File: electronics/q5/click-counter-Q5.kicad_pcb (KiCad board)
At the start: 2 copper layers, 42 x 54 mm, 93 parts, among them J1 USB-C power and DFU, Q1 Discharge FET, Q2 Charge FET, Q3 Charge enable, Q4 Charge enable hot gate, Q5 COUNT key level shift, SW1 COUNT / POWER, SW2 RESET COUNT / BOOT, SW3 MCU RESET, U1 STM32L072CBT6, U2 Li-ion charger, U3 3.20481V adjustable LDO, U4 Cell protector, U5 Push-pull temperature window, U6 OLED power slew switch, U7 System soft-power latch switch, U8 SPI F-RAM 32KiB

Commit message: WIP: Q5 design-lock routing iteration snapshot (not verified)
Co-Authored-By: Claude Opus 5.5 <noreply@anthropic.com>
Claude-Session: https://claude.ai/code/session_01UrkzLMrBi6iLPSL5SbMCA7
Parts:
- added C40: 4.7n, CountFidgetQ5:Capacitor_SMD_C_0603_1608Metric, B.Cu at (29.0, 37.0)
- added R38: 100k, CountFidgetQ5:Resistor_SMD_R_0603_1608Metric, B.Cu at (27.6, 37.3)
- SW1, SW2: footprint CountFidgetQ5:HanElectricity_CPG151101D13_MX_Plate -> CountFidgetQ5:SW_Hotswap_Kailh_MX_CPG151101S11; moved to B.Cu
- moved C29 15.0 mm to (28.9, 44.2)
- moved TP12 14.4 mm to (23.4, 43.6)
- moved R35 13.0 mm to (31.1, 30.0), turned to 180 degrees
- moved Q3 8.40 mm to (2.29, 47.5), turned to 90 degrees
- moved U3 7.72 mm to (39.3, 48.1)
- moved R11 6.20 mm to (2.47, 44.8), turned to 180 degrees
- moved TP11 6.00 mm to (28.3, 47.8)
- moved SW1 5.68 mm to (11.5, 40.8), turned to 90 degrees
- moved SW2 5.68 mm to (30.5, 40.8), turned to -90 degrees
- moved R10 4.60 mm to (6.40, 50.9)
- moved TP6 4.40 mm to (27.3, 40.2)
- moved C39 4.40 mm to (26.1, 37.0)
- moved SW3 4.22 mm to (33.6, 51.2)
- moved U5 4.00 mm to (9.28, 51.3), turned to 180 degrees
- moved C6 4.00 mm to (38.9, 40.6)
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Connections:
- D4 pad 1: SYS_ON -> VBUS_WAKE
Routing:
- net GND: track 368.8 -> 0.00 mm, vias 36 -> 0
- net VLOGIC: track 158.4 -> 0.00 mm, vias 4 -> 0
- net VBUS: track 123.4 -> 0.00 mm, vias 7 -> 0
- net SYS: track 103.0 -> 0.00 mm, vias 5 -> 0
- net BOOT_COUNT_RESET: track 92.0 -> 0.00 mm, vias 2 -> 0
- net SYS_LOAD: track 72.9 -> 0.00 mm, vias 3 -> 0
- net SYS_ON: track 71.5 -> 0.00 mm, vias 4 -> 0
- net CE_N: track 70.1 -> 0.00 mm, vias 2 -> 0
- net OLED_RESET_N: track 51.2 -> 0.00 mm, vias 1 -> 0
- net OLED_ENABLE: track 48.1 -> 0.00 mm
- net OLED_CS_N: track 47.1 -> 0.00 mm, vias 1 -> 0
- net CHG_STAT1: track 45.2 -> 0.00 mm, vias 2 -> 0
- net NRST: track 44.1 -> 0.00 mm, vias 4 -> 0
- net CELL_P: track 42.8 -> 0.00 mm
- net TEMP_SENSE: track 32.9 -> 0.00 mm, vias 2 -> 0
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- removed copper zone on B.Cu, net GND
- removed copper zone on F.Cu, net GND

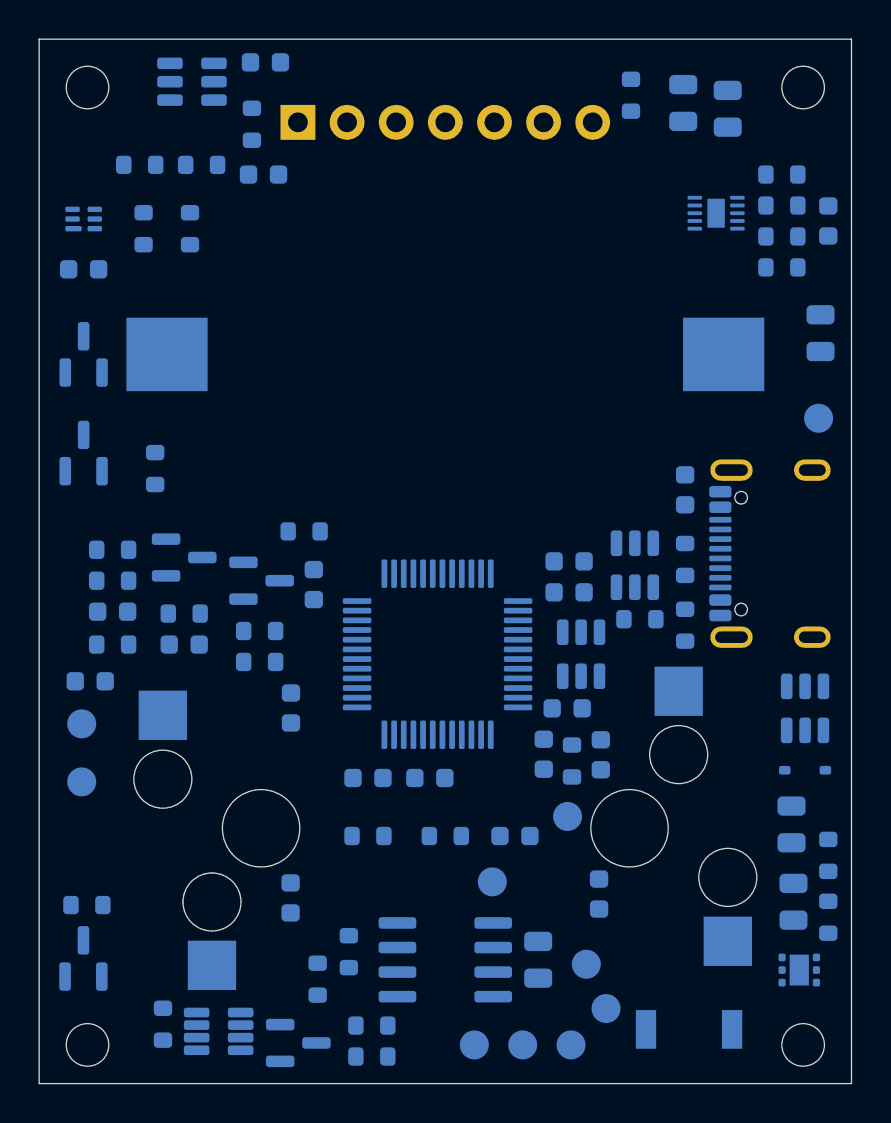
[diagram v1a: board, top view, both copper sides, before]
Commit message: Q5 design lock (electronics): hot-swap sockets, latch filter, 1.6 mm, clean native verification
Independent hardware/DFM and mechanical review follow-up:
- SW1/SW2 are now vendor-SMT Kailh-type MX hot-swap sockets (CPG151101S11-16,
  C41430893, rotated outward). The clicky switches clip into the printed
  plate and press in, so JLC can solder every part (variant B) and no switch
  soldering is needed in either variant. The board is 1.6 mm (MX pin length).
- R38 100k series + C40 4.7nF on U7 ON: VBUS hot-plug filter below the 6 V
  abs max and a contact-bounce bridge.
- BT1: +/- polarity silkscreen outside the holder body and paste kept off
  the inboard land; J1 slot rings 0.25 mm; silkscreen strokes >= 0.15 mm.
- 1.6 mm FR-4 / ENIG stackup; re-placed bottom side (sockets, SW3 reset
  switch, J1 +0.4 mm) and re-routed. Fresh KiCad 10.0.6: DRC 0/0/0, ERC 0,
  95 refs; 42/42 verifier corruptions rejected; circuit contract updated.
- Stock: 41/41 PCB MPNs, DS1 for full assembly, switches/header/screws at
  LCSC all pass. The LCSC order increment is now the `split` field.
- Exports for JLC quotation variants A (SMT; DS1 home-soldered) and B (SMT
  plus DS1/header THT), plus a loose-parts list.

Co-Authored-By: Claude Opus 5.5 <noreply@anthropic.com>
Claude-Session: https://claude.ai/code/session_01UrkzLMrBi6iLPSL5SbMCA7
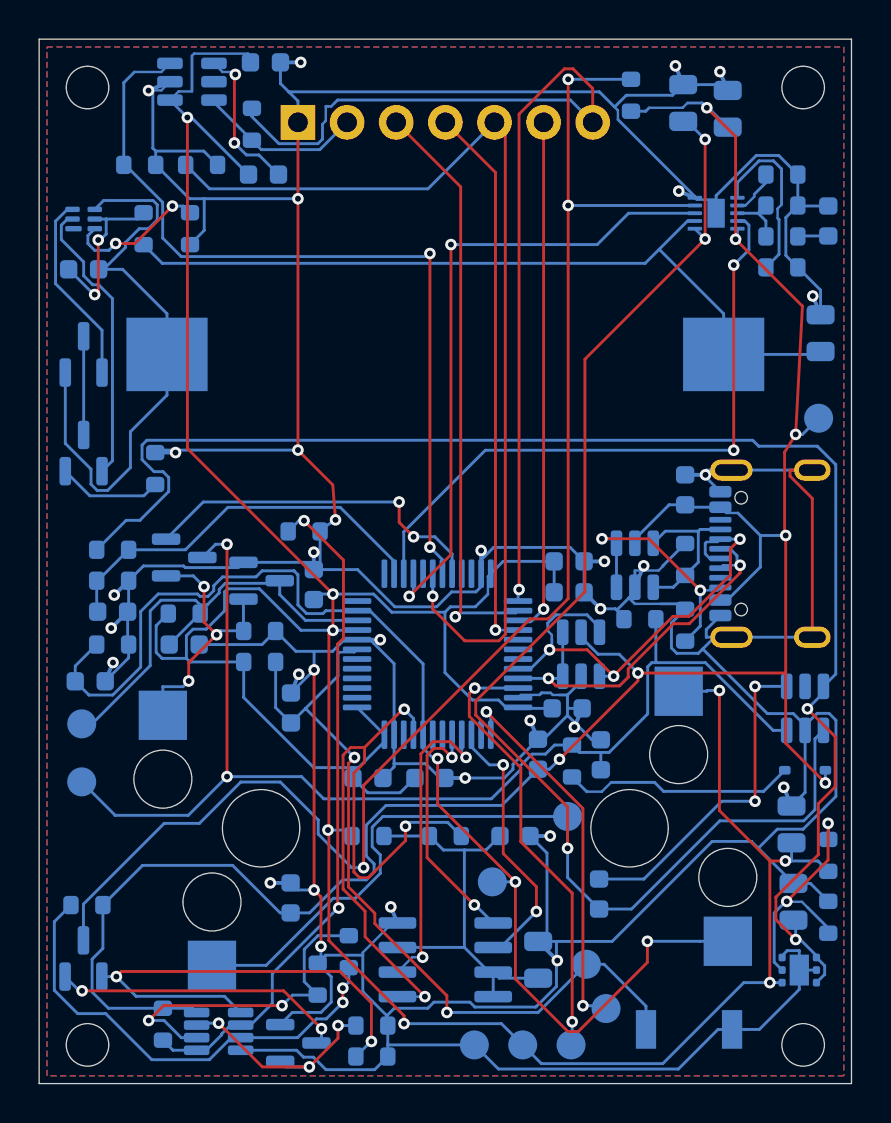
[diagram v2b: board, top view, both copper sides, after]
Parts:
- moved C39 0.30 mm to (25.8, 37.0)
- turned R10 to -90 degrees
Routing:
- net GND: track 0.00 -> 373.0 mm, vias 0 -> 32
- net VLOGIC: track 0.00 -> 172.9 mm, vias 0 -> 8
- net VBUS: track 0.00 -> 119.3 mm, vias 0 -> 7
- net SYS: track 0.00 -> 92.4 mm, vias 0 -> 3
- net CE_N: track 0.00 -> 76.7 mm, vias 0 -> 3
- net SYS_LOAD: track 0.00 -> 76.4 mm, vias 0 -> 2
- net BOOT_COUNT_RESET: track 0.00 -> 62.5 mm, vias 0 -> 3
- net SYS_ON: track 0.00 -> 61.4 mm, vias 0 -> 2
- net OLED_CS_N: track 0.00 -> 53.1 mm, vias 0 -> 1
- net OLED_RESET_N: track 0.00 -> 51.0 mm, vias 0 -> 1
- net OLED_ENABLE: track 0.00 -> 42.8 mm, vias 0 -> 2
- net CELL_P: track 0.00 -> 41.7 mm
- net NRST: track 0.00 -> 41.6 mm, vias 0 -> 2
- net FRAM_CS_N: track 0.00 -> 35.6 mm, vias 0 -> 3
- net TEMP_SENSE: track 0.00 -> 35.3 mm, vias 0 -> 2
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- added copper zone on B.Cu, net GND
- added copper zone on F.Cu, net GND

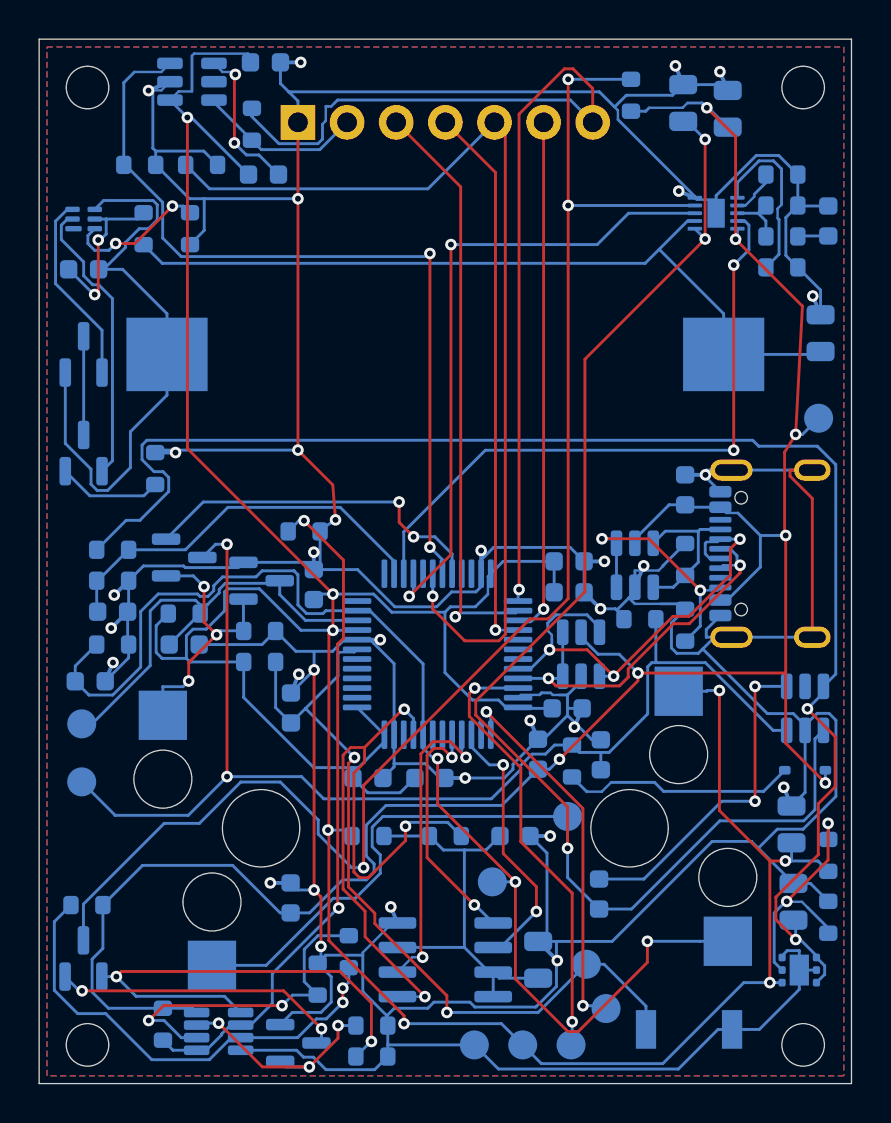
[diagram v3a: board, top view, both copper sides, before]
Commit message: First-order de-risking: U5 supply filter, 10 nF latch cap, JLC-corrected CPLs, DFU unplug rule
Three independent checks (datasheet pinouts, JLC EasyEDA footprints, dead-on-arrival
review) found no pinout, footprint or DOA defect. Changes from their findings:
R39 1k + C9 filter U5's 6 V abs-max supply from VBUS hot-plug ringing; C40 10 nF
(min latch press 10.5 ms typ); JLC-corrected CPL files and a preview checklist;
flasher warns to reset a unit left in DFU before unplugging. Board re-routed:
DRC/ERC/parity zero, no via-to-land gaps; emulator 0 failures; stock 43/43.

Co-Authored-By: Claude Opus 5.5 <noreply@anthropic.com>
Claude-Session: https://claude.ai/code/session_01UrkzLMrBi6iLPSL5SbMCA7
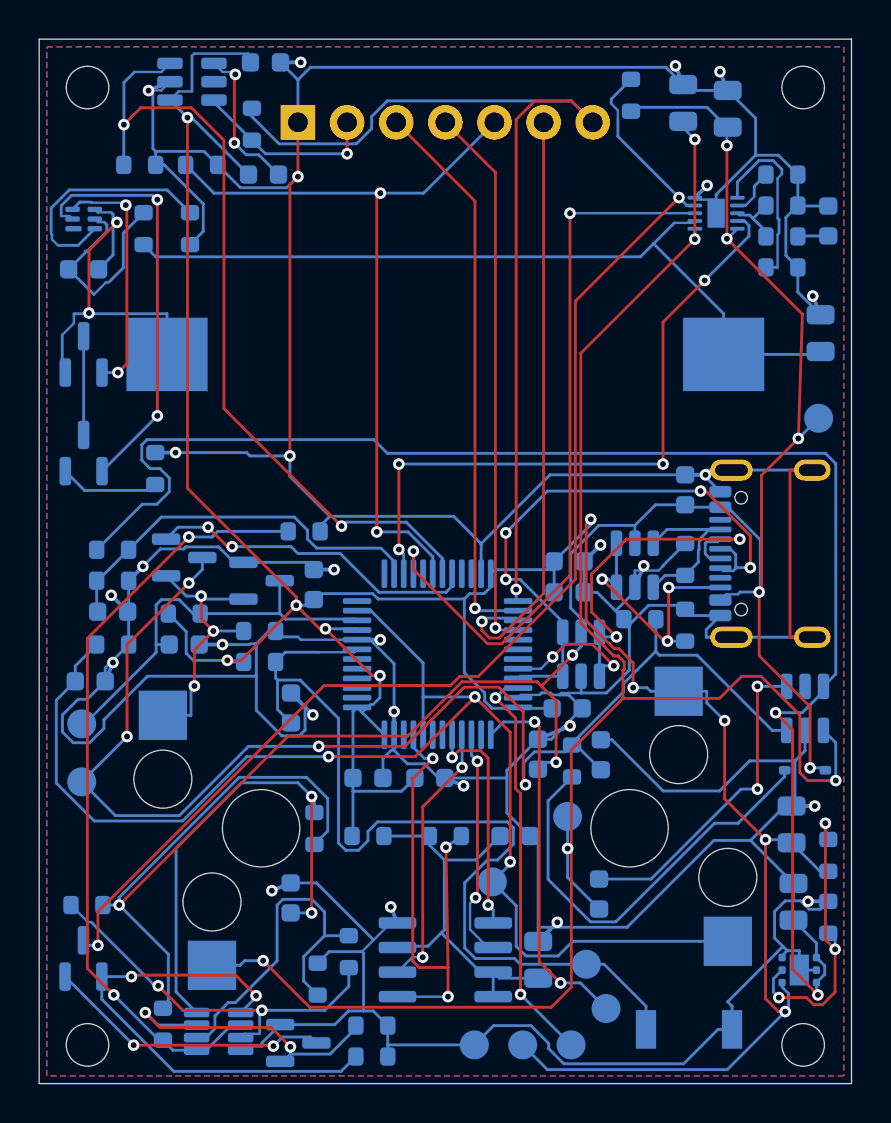
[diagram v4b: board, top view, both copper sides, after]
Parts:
- added R39: 1k, CountFidgetQ5:Resistor_SMD_R_0603_1608Metric, B.Cu at (14.2, 40.8)
- C40: value 4.7n -> 10n
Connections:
- C9 pad 1: VBUS -> U5_VCC
- U5 pad 8: VBUS -> U5_VCC
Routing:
- net U5_VCC: track 0.00 -> 25.6 mm, vias 0 -> 2
- net VLOGIC: track 172.9 -> 154.2 mm, vias 8 -> 10
- net CE_N: track 76.7 -> 65.3 mm, vias 3 -> 2
- net OLED_RESET_N: track 51.0 -> 40.0 mm, vias 1 -> 2
- net CELL_N_RAW: track 30.7 -> 20.0 mm, vias 0 -> 2
- net USB_DP: track 20.4 -> 30.9 mm, vias 2 -> 4
- net VBUS_WAKE: track 12.2 -> 22.4 mm
- net FRAM_CS_N: track 35.6 -> 26.1 mm
- net BOOT_COUNT_RESET: track 62.5 -> 70.1 mm
- net VBUS: track 119.3 -> 126.9 mm, vias 7 -> 8
- net COUT: track 14.9 -> 21.7 mm, vias 0 -> 2
- net NRST: track 41.6 -> 48.0 mm, vias 2 -> 0
- net SYS_ON: track 61.4 -> 67.6 mm, vias 2 -> 4
- net VMINUS: track 7.43 -> 12.4 mm, vias 2 -> 0
- net CHG_STAT2: track 33.6 -> 38.5 mm
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
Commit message: Move nine part types to JLC Basic; 16 Extended types remain, each justified
R4 18k (16.7 mA charge), temperature window 56k/82k/18k/12k (7.26-35.83 C),
R32 75 ohm, Q1/Q2 AO3400A, 2.2 uF and 10 uF 50 V 0805 capacitors. Fresh
ERC/DRC/parity on unchanged routing, stock 42/42, exports, JLC footprint
fit and pin names, power/latch checks re-run. About $28 less per order.

Co-Authored-By: Claude Opus 5.5 <noreply@anthropic.com>
Claude-Session: https://claude.ai/code/session_01UrkzLMrBi6iLPSL5SbMCA7
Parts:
- R10: value 57.6k -> 56k
- R11: value 115k -> 82k
- R12: value 24.3k -> 18k
- R13: value 16.2k -> 12k
- R32: value 68 -> 75
- R4: value 16.5k -> 18k
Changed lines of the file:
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@@
 			)
 		)
-		(property "Description" "; exact same-device reel suffix -13; no electrical polarity change"
+		(property "Description" "AO3400A: SOT-23 1 G / 2 S / 3 D, 30 V, 48 mOhm max at VGS 2.5 V; BQ29700 FET per TI Fig. 9-1"
 			(at 0 0 270)
 			(layer "B.Fab")
@@
 			)
 		)
-		(property "MPN" "DMN2056U-13"
+		(property "MPN" "AO3400A"
 			(at 0 0 0)
 			(layer "B.SilkS")
@@
 			)
 		)
-		(property "Value" "16.5k"
+		(property "Value" "18k"
 			(at 0 -1.43 180)
 			(layer "B.Fab")
@@
 			)
 		)
-		(property "MPN" "RC0603FR-0716K5L"
+		(property "MPN" "0603WAF1802T5E"
 			(at 0 0 0)
 			(layer "B.SilkS")
@@
 			)
 		)
-		(property "Description" "10uF package rail bulk; include all MCU/FRAM/module capacitance in regulator stability and startup review; effective capacitance unmeasured"
+		(property "Description" "10 uF, 50 V, X5R, 0805; effective >=1 uF at 4.5 V"
 			(at 0 0 270)
 			(layer "B.Fab")
@@
 			)
 		)
-		(property "MPN" "GRM21BR61E106KA73L"
+		(property "MPN" "GRM21BR61H106KE43L"
 			(at 0 0 0)
 			(layer "B.SilkS")
@@
 			)
 		)
-		(property "Description" "10uF25V X5R; require>=6.8uF effective for proposed memory ramp budget"
+		(property "Description" "10 uF 50 V X5R; require >=6.8 uF effective at the memory rail (measure on the first article)"
 			(at 0 0 270)
 			(layer "B.Fab")
@@
 			)
 		)
-		(property "MPN" "GRM21BR61E106KA73L"
+		(property "MPN" "GRM21BR61H106KE43L"
 			(at 0 0 0)
 			(layer "B.SilkS")
@@
 			)
 		)
-		(property "Description" "10 uF, 25 V, X5R; effective >=1 uF at 4.5 V"
+		(property "Description" "10 uF, 50 V, X5R, 0805; effective >=1 uF at 4.5 V"
 			(at 0 0 270)
 			(layer "B.Fab")
@@
 			)
 		)
-		(property "MPN" "GRM21BR61E106KA73L"
+		(property "MPN" "GRM21BR61H106KE43L"
 			(at 0 0 0)
 			(layer "B.SilkS")
@@
 			)
 		)
-		(property "Value" "115k"
+		(property "Value" "82k"
 			(at 0 -1.43 0)
 			(layer "B.Fab")
@@
 			)
 		)
-		(property "MPN" "0603WAF1153T5E"
+		(property "MPN" "0603WAF8202T5E"
 			(at 0 0 0)
 			(layer "B.SilkS")
@@
 			)
 		)
-		(property "Value" "24.3k"
+		(property "Value" "18k"
 			(at 0 -1.43 270)
 			(layer "B.Fab")
@@
 			)
 		)
-		(property "MPN" "RC0603FR-0724K3L"
+		(property "MPN" "0603WAF1802T5E"
 			(at 0 0 0)
 			(layer "B.SilkS")
@@
 			)
 		)
-		(property "Value" "16.2k"
+		(property "Value" "12k"
 			(at 0 -1.43 270)
 			(layer "B.Fab")
@@
 			)
 		)
-		(property "MPN" "0603WAF1622T5E"
+		(property "MPN" "0603WAF1202T5E"
 			(at 0 0 0)
 			(layer "B.SilkS")
@@
 			)
 		)
-		(property "Description" "; exact same-device reel suffix -13; no electrical polarity change"
+		(property "Description" "AO3400A: SOT-23 1 G / 2 S / 3 D, 30 V, 48 mOhm max at VGS 2.5 V; BQ29700 FET per TI Fig. 9-1"
 			(at 0 0 270)
 			(layer "B.Fab")
@@
 			)
 		)
-		(property "MPN" "DMN2056U-13"
+		(property "MPN" "AO3400A"
 			(at 0 0 0)
 			(layer "B.SilkS")
@@
 			)
 		)
-		(property "Description" "2.2 uF, 25 V, X7R; effective >=1 uF at 5 V"
+		(property "Description" "2.2 uF, 50 V, X5R, 0805; effective >=1 uF at 5 V"
 			(at 0 0 270)
 			(layer "B.Fab")
@@
 			)
 		)
-		(property "MPN" "GRM21BR71E225KE11L"
+		(property "MPN" "CL21A225KBQNNNE"
 			(at 0 0 0)
 			(layer "B.SilkS")
@@
 			)
 		)
-		(property "Value" "68"
+		(property "Value" "75"
 			(at 0 -1.43 180)
 			(layer "B.Fab")
@@
 			)
 		)
-		(property "Description" "1%; controlled memory rail RC"
+		(property "Description" "1%; controlled memory rail RC (75 ohm with C30)"
 			(at 0 0 180)
 			(layer "B.Fab")
@@
 			)
 		)
-		(property "MPN" "0603WAF680JT5E"
+		(property "MPN" "0603WAF750JT5E"
 			(at 0 0 0)
 			(layer "B.SilkS")
@@
 			)
 		)
-		(property "Description" "2.2 uF, 25 V, X7R"
+		(property "Description" "2.2 uF, 50 V, X5R, 0805; effective >=1 uF at 5 V"
 			(at 0 0 270)
 			(layer "B.Fab")
@@
 			)
 		)
-		(property "MPN" "GRM21BR71E225KE11L"
+		(property "MPN" "CL21A225KBQNNNE"
 			(at 0 0 0)
 			(layer "B.SilkS")
@@
 			)
 		)
-		(property "Value" "57.6k"
+		(property "Value" "56k"
 			(at 0 -1.43 90)
 			(layer "B.Fab")
@@
 			)
 		)
-		(property "MPN" "RC0603FR-0757K6L"
+		(property "MPN" "0603WAF5602T5E"
 			(at 0 0 0)
 			(layer "B.SilkS")
@@
 			)
 		)
-		(property "Description" ""
+		(property "Description" "2.2 uF, 50 V, X5R, 0805; effective >=1 uF at 5 V"
 			(at 0 0 270)
 			(layer "B.Fab")
@@
 			)
 		)
-		(property "MPN" "GRM21BR71E225KE11L"
+		(property "MPN" "CL21A225KBQNNNE"
 			(at 0 0 0)
 			(layer "B.SilkS")
